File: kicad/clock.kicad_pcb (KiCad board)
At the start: 4 copper layers, 110 x 110 mm, 187 parts, among them J1 USB4160-03-0230-C, J10 Knob: EM14 enc+SW (top face), J11 Radio-off toggle (rear), J12 NeoPixel ext (5V/DATA/GND, po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, J2 PROG, J3 Speaker DMA58-4 (4R), J6 DM3AT-SF-PEJM5, J7 Sensor board (BME688+TSL2591+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, J9 Wake COB 12V (warm+cool), M1 X40.879, Q1 2N7002, Q2 AO3401A, Q3 2N7002, Q4 AO3401A, Q6 AO3400A, Q7 AO3400A, Q8 2N7002, Q9 AO3401A, SW1 RESET, SW2 BOOT, U1 CH224K, U10 LTC4412ES6, U11 TB6612FNG, U12 TB6612FNG, U13 MCP23017, U14 QRE1113GR, U15 SN74AHCT1G125, U16 USBLC6-2SC6, U2 LT3652EMSE, U3 HY2111-GB, U4 AOSD32334C, U5 TPS61023, U6 TLV62569DBVR, U7 TPS55340PWPR, U8 ESP32-S3-WROOM-1-N8R8, U9 TAS5760MDAPR, Y1 32.768kHz

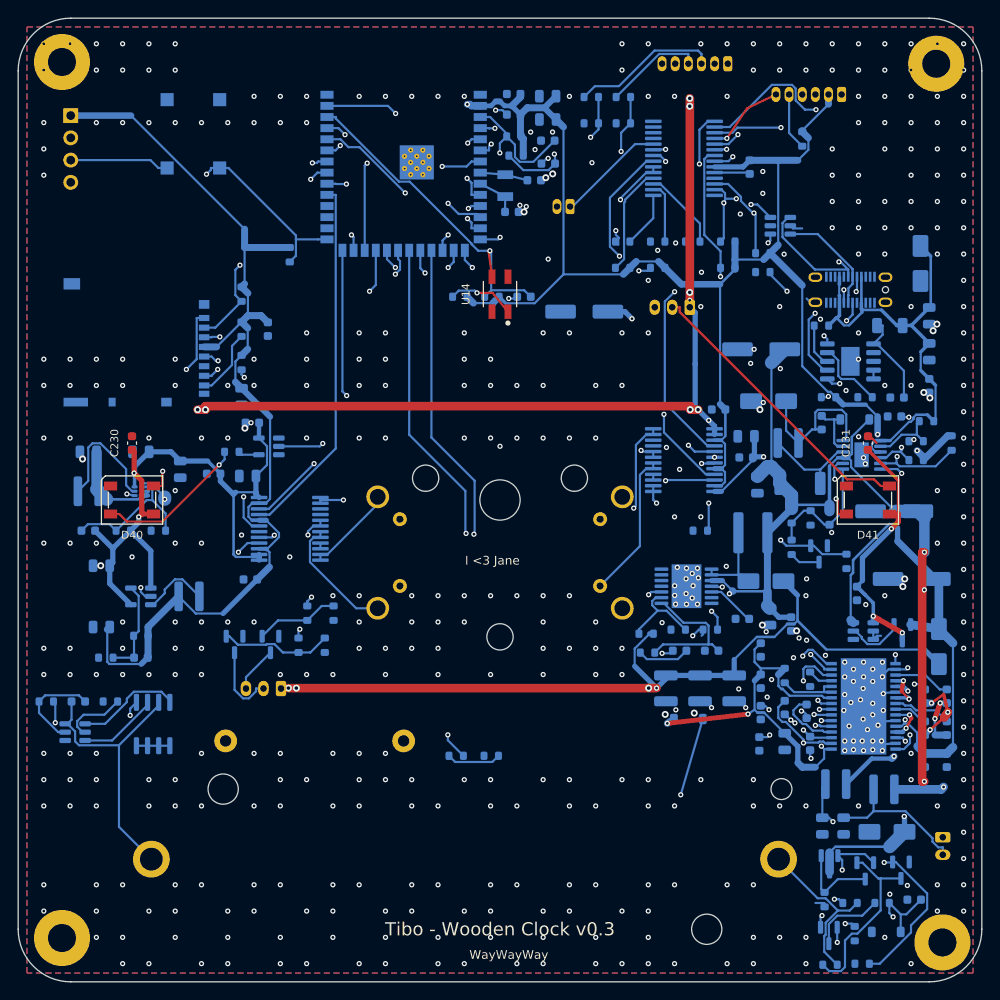
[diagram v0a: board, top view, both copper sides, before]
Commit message: move LED on PCB outwards
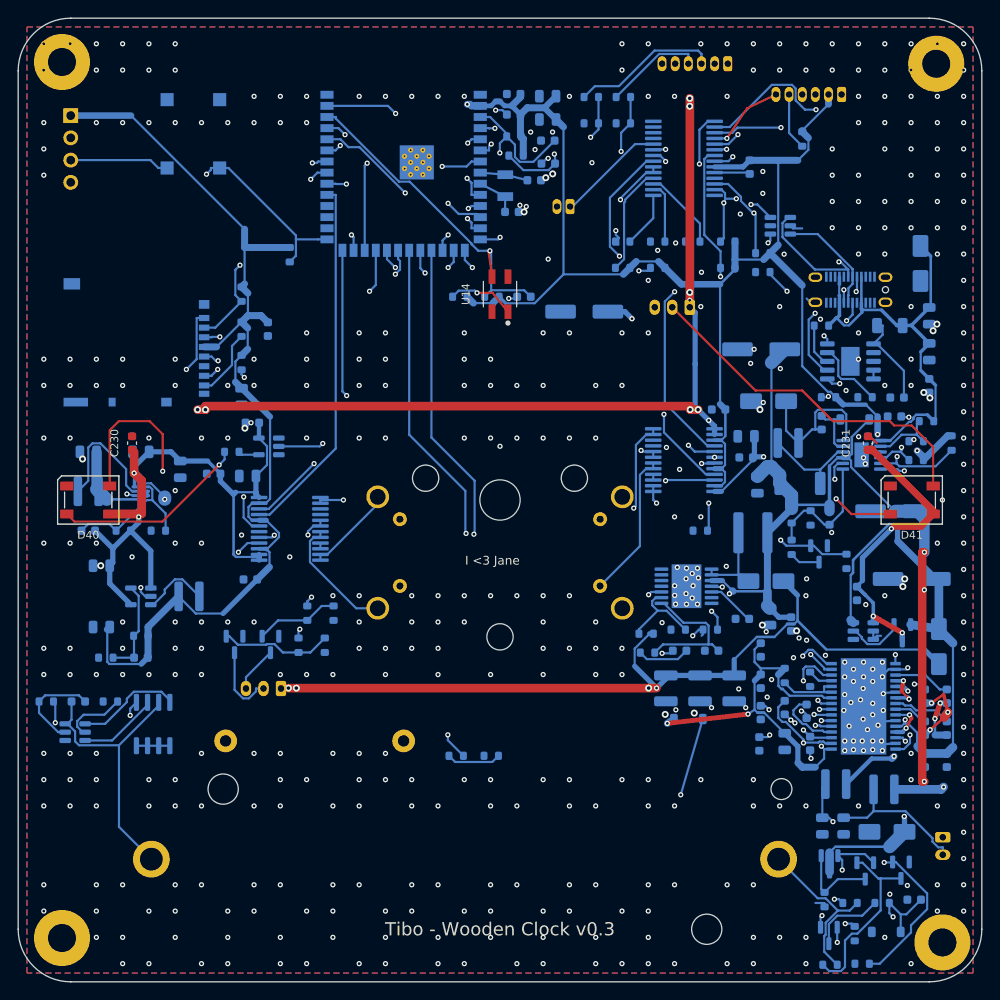
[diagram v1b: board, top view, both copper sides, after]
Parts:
- moved D40 5.00 mm to (8.00, 55.0)
- moved D41 5.00 mm to (102.0, 55.0)
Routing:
- net Net-(D40-DOUT): track 85.2 -> 104.3 mm
- net Net-(D41-DOUT): track 33.5 -> 40.8 mm
- net +5V: track 267.1 -> 273.5 mm
- net Net-(D40-DIN): track 17.2 -> 22.2 mm
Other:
- board text removed: "WayWayWay"
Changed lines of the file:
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@@
 	(footprint "LED_SMD:LED_SK6812_PLCC4_5.0x5.0mm_P3.2mm"
 		(layer "F.Cu")
-		(at 97 55)
+		(at 102 55)
 		(descr "5.0mm x 5.0mm Addressable RGB LED NeoPixel, https://cdn-shop.adafruit.com/product-files/1138/SK6812+LED+datasheet+.pdf")
 		(tags "LED RGB NeoPixel PLCC-4 5050")
@@
 	(footprint "LED_SMD:LED_SK6812_PLCC4_5.0x5.0mm_P3.2mm"
 		(layer "F.Cu")
-		(at 13 55)
+		(at 8 55)
 		(descr "5.0mm x 5.0mm Addressable RGB LED NeoPixel, https://cdn-shop.adafruit.com/product-files/1138/SK6812+LED+datasheet+.pdf")
 		(tags "LED RGB NeoPixel PLCC-4 5050")
@@
 		)
 	)
-	(gr_text "WayWayWay"
-		(at 51.5 107.5 0)
-		(layer "F.SilkS")
-		(effects
-			(font
-				(size 1 1)
-				(thickness 0.1)
-			)
-			(justify left bottom)
-		)
-	)
 	(gr_text "Tibo - Wooden Clock v0.3"
 		(at 55 104 0)
@@
 	)
 	(via
-		(at 104.925 53.925)
+		(at 105.5 55)
 		(size 0.6)
 		(drill 0.3)
@@
 	)
 	(segment
-		(start 21.38 44.69)
-		(end 21.38 44.29)
+		(start 97 49.275)
+		(end 97.481257 49.275)
 		(width 1)
 		(layer "F.Cu")
@@
 	)
 	(segment
-		(start 100.45 52.725)
-		(end 97 49.275)
-		(width 0.4)
+		(start 21.38 44.69)
+		(end 21.38 44.29)
+		(width 1)
 		(layer "F.Cu")
 		(net "+5V")
 	)
 	(segment
-		(start 99.45 56.6)
-		(end 100.45 56.6)
-		(width 0.6)
+		(start 97.481257 49.275)
+		(end 104.45 56.243742)
+		(width 0.8)
 		(layer "F.Cu")
 		(net "+5V")
@@
 		(start 13.2372 51.9283)
 		(end 13.2372 49.5122)
-		(width 0.6)
+		(width 1)
 		(layer "F.Cu")
 		(net "+5V")
@@
 	)
 	(segment
-		(start 15.45 56.6)
-		(end 14.95 56.6)
-		(width 0.6)
-		(layer "F.Cu")
-		(net "+5V")
-	)
-	(segment
 		(start 13.2372 49.5122)
 		(end 13 49.275)
@@
 	)
 	(segment
-		(start 100.45 56.6)
-		(end 100.45 52.725)
-		(width 0.3)
+		(start 13.6281 56.6)
+		(end 13.7642 56.7361)
+		(width 1)
 		(layer "F.Cu")
 		(net "+5V")
 	)
 	(segment
-		(start 100.45 57.51)
-		(end 100.45 56.6)
-		(width 0.6)
+		(start 99.6764 58.2836)
+		(end 99.96 58)
+		(width 0.3)
 		(layer "F.Cu")
 		(net "+5V")
@@
 	)
 	(segment
-		(start 14.95 56.6)
-		(end 14.0986 56.6)
-		(width 0.6)
+		(start 21.38 44.29)
+		(end 76.71 44.29)
+		(width 1)
 		(layer "F.Cu")
 		(net "+5V")
 	)
 	(segment
-		(start 21.38 44.29)
-		(end 76.71 44.29)
+		(start 10.45 56.6)
+		(end 13.6281 56.6)
 		(width 1)
 		(layer "F.Cu")
@@
 		(start 14.0986 52.7897)
 		(end 13.2372 51.9283)
-		(width 0.6)
+		(width 1)
+		(layer "F.Cu")
+		(net "+5V")
+	)
+	(segment
+		(start 99.96 58)
+		(end 103.05 58)
+		(width 0.8)
 		(layer "F.Cu")
 		(net "+5V")
@@
 		(start 14.0986 56.6)
 		(end 14.0986 52.7897)
-		(width 0.6)
+		(width 1)
 		(layer "F.Cu")
 		(net "+5V")
 	)
 	(segment
-		(start 99.6764 58.2836)
-		(end 100.45 57.51)
-		(width 0.6)
+		(start 104.45 56.243742)
+		(end 104.45 56.6)
+		(width 0.8)
+		(layer "F.Cu")
+		(net "+5V")
+	)
+	(segment
+		(start 103.05 58)
+		(end 104.45 56.6)
+		(width 0.8)
 		(layer "F.Cu")
 		(net "+5V")
@@
 	)
 	(segment
-		(start 94.55 56.6)
-		(end 93.55 56.6)
+		(start 16.4958 51.716)
+		(end 16.4958 47.4958)
 		(width 0.25)
 		(layer "F.Cu")
@@
 	)
 	(segment
-		(start 93.55 55.0409)
-		(end 93.55 56.6)
+		(start 16.4958 47.4958)
+		(end 15 46)
 		(width 0.25)
 		(layer "F.Cu")
@@
 	)
 	(segment
-		(start 16.45 53.4)
-		(end 16.45 51.7618)
+		(start 93.3691 54.86)
+		(end 95.1091 56.6)
 		(width 0.25)
 		(layer "F.Cu")
@@
 	)
 	(segment
-		(start 93.3691 54.86)
-		(end 93.55 55.0409)
+		(start 15 46)
+		(end 11.5 46)
 		(width 0.25)
 		(layer "F.Cu")
@@
 	)
 	(segment
-		(start 15.45 53.4)
-		(end 16.45 53.4)
+		(start 95.1091 56.6)
+		(end 99.55 56.6)
 		(width 0.25)
 		(layer "F.Cu")
@@
 		(net "Net-(D40-DOUT)")
 	)
+	(segment
+		(start 10.45 47.05)
+		(end 10.45 53.4)
+		(width 0.25)
+		(layer "F.Cu")
+		(net "Net-(D40-DOUT)")
+	)
+	(segment
+		(start 11.5 46)
+		(end 10.45 47.05)
+		(width 0.25)
+		(layer "F.Cu")
+		(net "Net-(D40-DOUT)")
+	)
 	(via
 		(at 16.4958 51.716)
@@
 	)
 	(segment
-		(start 75.5139 33)
-		(end 75.5139 33.5313)
+		(start 89.5 42.5)
+		(end 93 46)
 		(width 0.25)
 		(layer "F.Cu")
@@
 	)
 	(segment
-		(start 75.5139 33.5313)
-		(end 94.6326 52.65)
+		(start 104.45 48.95)
+		(end 104.45 53.4)
 		(width 0.25)
 		(layer "F.Cu")
@@
 	)
 	(segment
-		(start 94.6326 52.65)
-		(end 97.7 52.65)
+		(start 100 46.5)
+		(end 102 46.5)
 		(width 0.25)
 		(layer "F.Cu")
@@
 	)
 	(segment
-		(start 97.7 52.65)
-		(end 98.45 53.4)
+		(start 99.5 46)
+		(end 100 46.5)
 		(width 0.25)
 		(layer "F.Cu")
@@
 	)
 	(segment
-		(start 99.45 53.4)
-		(end 98.45 53.4)
+		(start 102 46.5)
+		(end 104.45 48.95)
 		(width 0.25)
 		(layer "F.Cu")
@@
 	(segment
 		(start 74.6639 33)
-		(end 75.5139 33)
+		(end 84.1639 42.5)
+		(width 0.25)
+		(layer "F.Cu")
+		(net "Net-(D41-DOUT)")
+	)
+	(segment
+		(start 84.1639 42.5)
+		(end 89.5 42.5)
+		(width 0.25)
+		(layer "F.Cu")
+		(net "Net-(D41-DOUT)")
+	)
+	(segment
+		(start 93 46)
+		(end 99.5 46)
 		(width 0.25)
 		(layer "F.Cu")
@@
 	)
 	(segment
-		(start 11.55 56.6)
-		(end 12.4111 57.4611)
+		(start 16.472 57.4611)
+		(end 22.9381 50.995)
 		(width 0.25)
 		(layer "F.Cu")
@@
 	)
 	(segment
-		(start 12.4111 57.4611)
+		(start 6.4111 57.4611)
 		(end 16.472 57.4611)
 		(width 0.25)
@@
 	)
 	(segment
-		(start 10.55 56.6)
-		(end 11.55 56.6)
-		(width 0.25)
-		(layer "F.Cu")
-		(net "Net-(D40-DIN)")
-	)
-	(segment
-		(start 16.472 57.4611)
-		(end 22.9381 50.995)
+		(start 5.55 56.6)
+		(end 6.4111 57.4611)
 		(width 0.25)
 		(layer "F.Cu")
@@
 	)
 	(via
-		(at 100.8542 51.9593)
+		(at 101.15675 51.6777)
 		(size 0.6)
 		(drill 0.3)
@@
 	)
 	(segment
-		(start 100.8884 45.5484)
-		(end 100.8027 45.4627)
+		(start 100.5726 51.6777)
+		(end 100.3633 51.4684)
 		(width 0.25)
 		(layer "B.Cu")
@@
 	)
 	(segment
-		(start 100.3633 51.4684)
-		(end 100.8542 51.9593)
+		(start 101.15675 51.6777)
+		(end 100.5726 51.6777)
+		(width 0.25)
+		(layer "B.Cu")
+		(net "Net-(U2-TIMER)")
+	)
+	(segment
+		(start 100.8884 45.5484)
+		(end 100.8027 45.4627)
 		(width 0.25)
 		(layer "B.Cu")
@@
 	)
 	(segment
-		(start 98.4286 51.4684)
-		(end 100.3633 51.4684)
+		(start 100.3633 51.4684)
+		(end 98.4286 51.4684)
 		(width 0.25)
 		(layer "B.Cu")
@@
 	)
 	(segment
+		(start 101.15675 51.6777)
+		(end 101.15675 51.65675)
+		(width 0.25)
+		(layer "In1.Cu")
+		(net "Net-(U2-TIMER)")
+	)
+	(segment
 		(start 101.6738 51.1397)
 		(end 101.6738 45.5484)
@@
 	)
 	(segment
-		(start 100.8542 51.9593)
+		(start 101.15675 51.65675)
 		(end 101.6738 51.1397)
 		(width 0.25)
